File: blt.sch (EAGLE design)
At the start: 46 parts, among them IC1 TL074D, IC2 TL074D

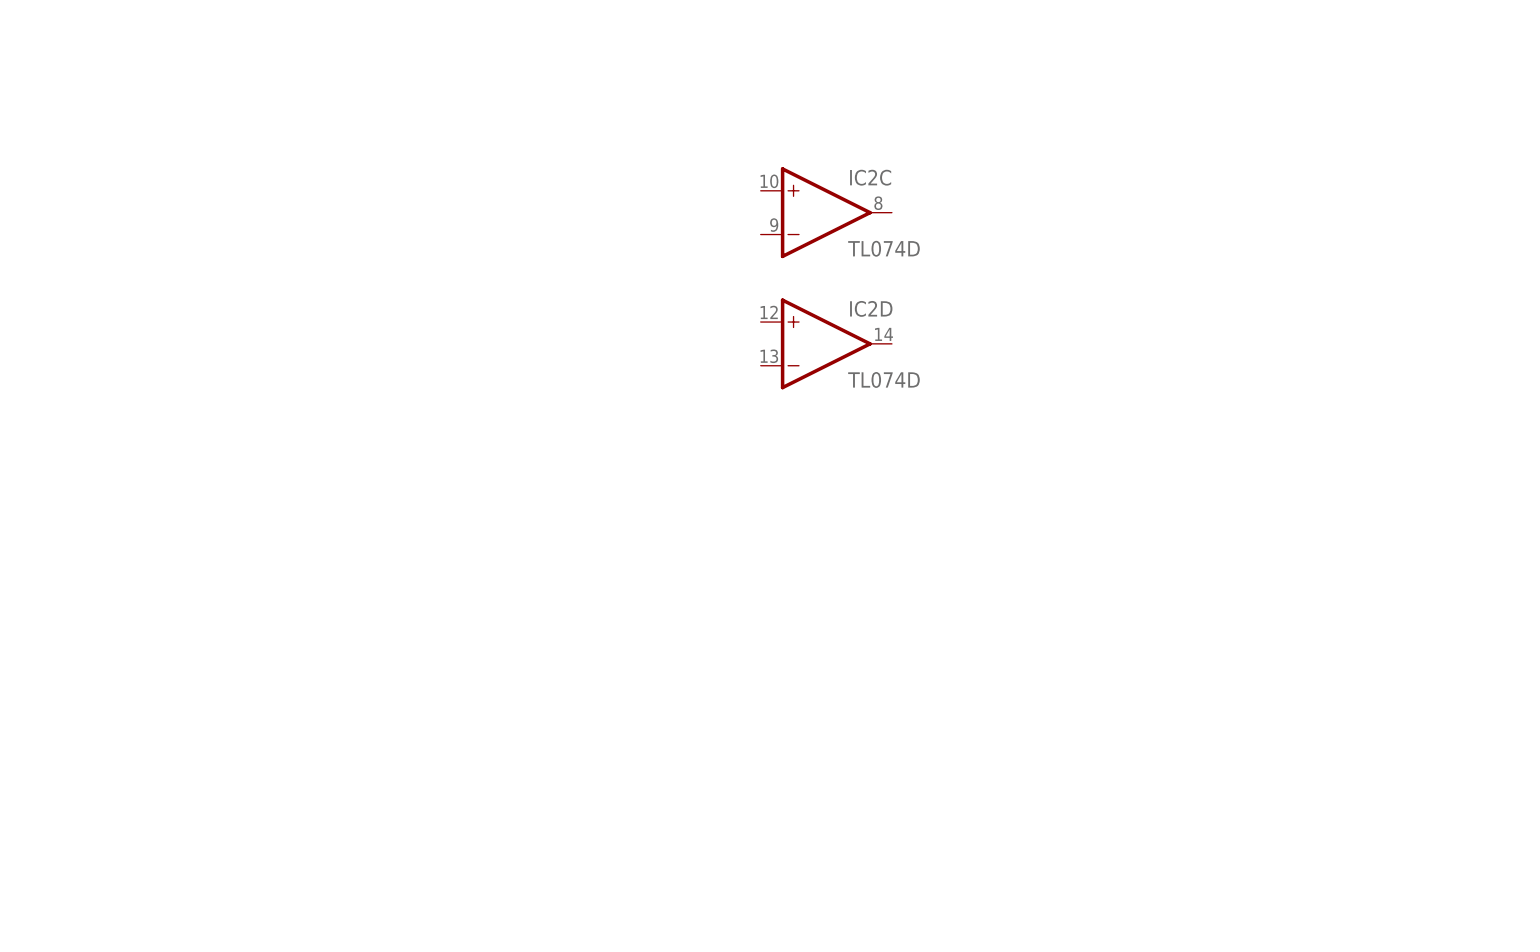
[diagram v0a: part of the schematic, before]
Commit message: добавлен балансный приёмник
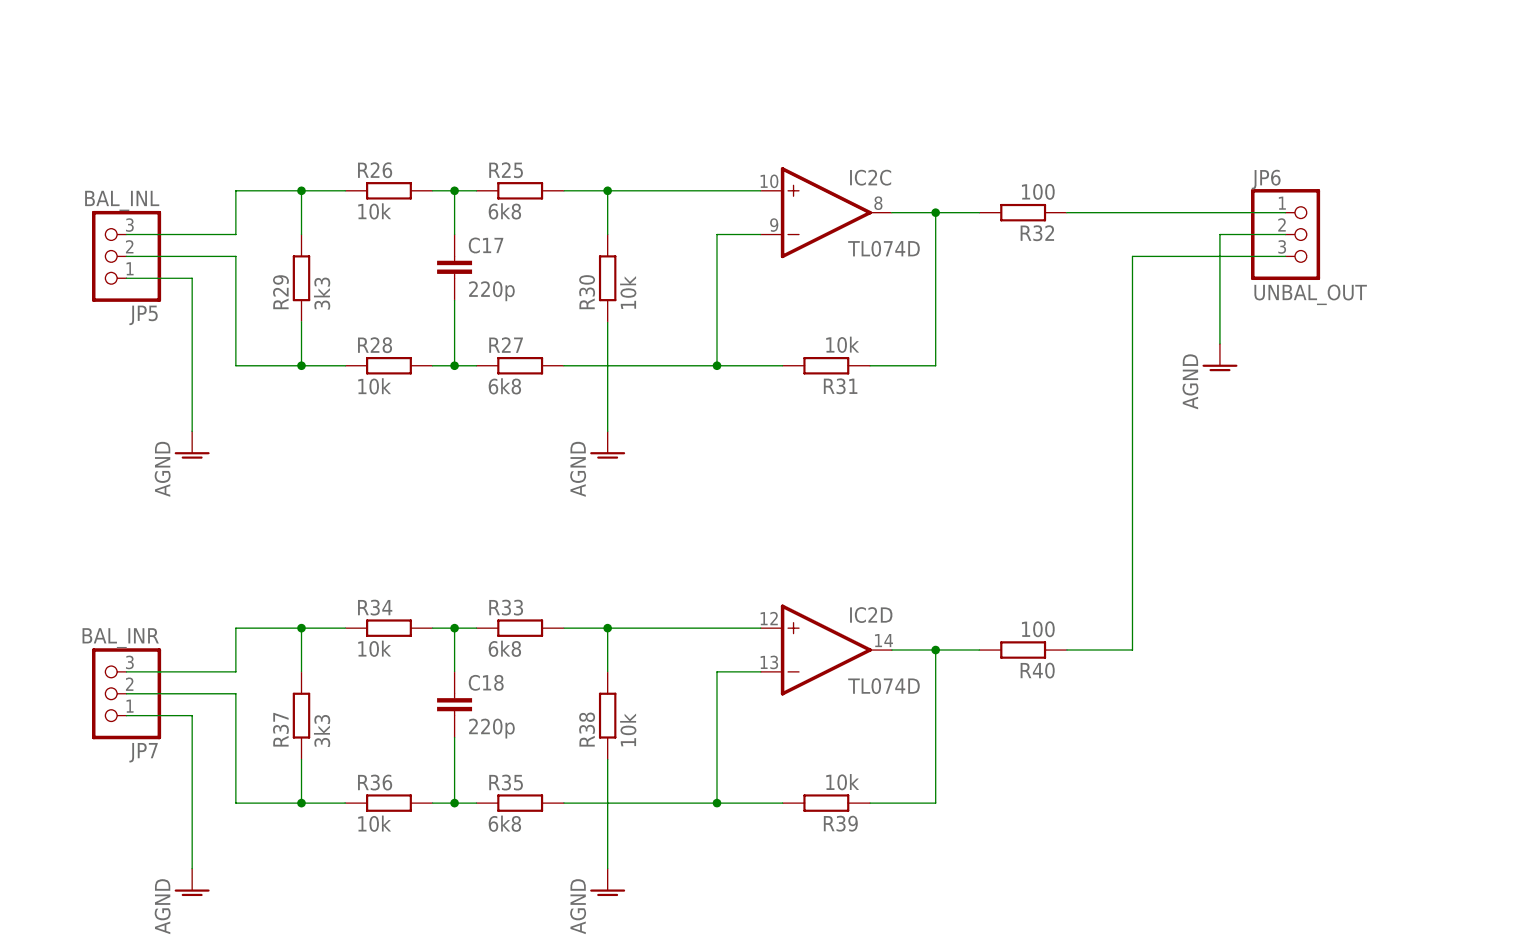
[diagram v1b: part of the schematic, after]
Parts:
- added C17, C18: 220p, rcl:C-EUC1206
- added JP5: BAL_INL, pinhead:PINHD-1X3
- added JP6: UNBAL_OUT, pinhead:PINHD-1X3
- added JP7: BAL_INR, pinhead:PINHD-1X3
- added R25, R27, R33, R35: 6k8, rcl:R-EU_R1206
- added R26, R28, R30, R31, R34, R36, R38, R39: 10k, rcl:R-EU_R1206
- added R29, R37: 3k3, rcl:R-EU_R1206
- added R32, R40: 100, rcl:R-EU_R1206
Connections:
- new net N$23: JP5.3, R26.1, R29.2
- new net N$24: JP5.2, R28.1, R29.1
- new net N$25: C17.1, R25.1, R26.2
- new net N$26: C17.2, R27.1, R28.2
- new net N$27: IC2C.+IN, R25.2, R30.2
- new net N$28: IC2C.-IN, R27.2, R31.2
- new net N$29: IC2C.OUT, R31.1, R32.2
- new net N$30: IC2D.OUT, R39.1, R40.2
- new net N$31: JP6.1, R32.1
- new net N$32: JP7.3, R34.1, R37.2
- new net N$33: JP7.2, R36.1, R37.1
- new net N$34: C18.1, R33.1, R34.2
- new net N$35: C18.2, R35.1, R36.2
- new net N$36: IC2D.+IN, R33.2, R38.2
- new net N$37: IC2D.-IN, R35.2, R39.2
- new net N$38: JP6.3, R40.1
- net AGND: now also JP5.1, JP6.2, JP7.1, R30.1, R38.1
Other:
- moved on the sheet: IC2D
